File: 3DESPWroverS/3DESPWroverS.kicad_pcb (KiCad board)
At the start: 2 copper layers, 40 x 40 mm, 9 parts, among them J1 Conn_02x03_Odd_Even, J2 Conn_01x01, J3 Conn_01x01, J4 Conn_01x01, J5 Conn_01x01, J6 Conn_01x01, J7 Conn_01x01, J8 Conn_01x01, J9 Conn_01x01

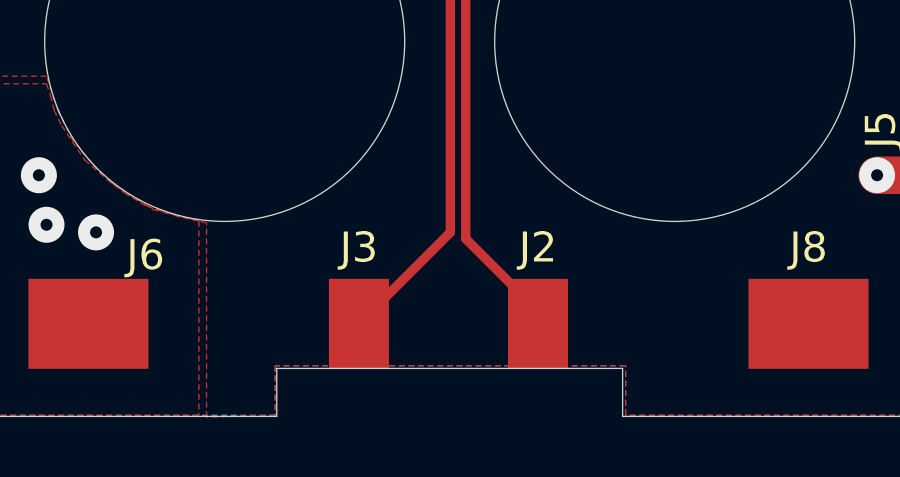
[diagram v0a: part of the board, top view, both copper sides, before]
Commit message: Correction to 3.3v regulator connection
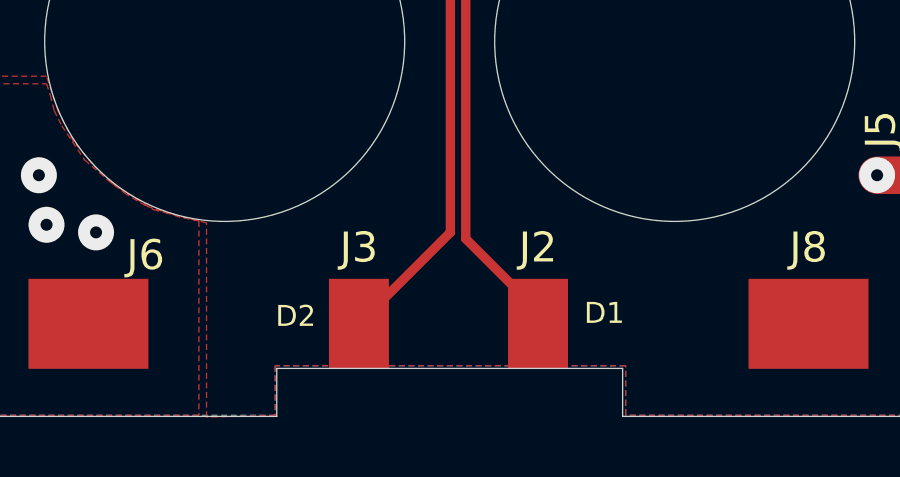
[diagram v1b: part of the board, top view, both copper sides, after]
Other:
- board text added: "D1"
- board text added: "D2"
- board text added: "GND"
- board text added: "VCC"
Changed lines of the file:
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@@
   (general
     (thickness 1.6)
-    (drawings 66)
+    (drawings 72)
     (tracks 31)
     (zones 0)
@@
       (effects (font (size 1 1) (thickness 0.15)) (justify mirror))
     )
+    (fp_line (start 4.35 1.8) (end -1.8 1.8) (layer B.CrtYd) (width 0.05))
+    (fp_line (start 4.35 -6.85) (end 4.35 1.8) (layer B.CrtYd) (width 0.05))
+    (fp_line (start -1.8 -6.85) (end 4.35 -6.85) (layer B.CrtYd) (width 0.05))
+    (fp_line (start -1.8 1.8) (end -1.8 -6.85) (layer B.CrtYd) (width 0.05))
+    (fp_line (start -1.33 1.33) (end 0 1.33) (layer B.SilkS) (width 0.12))
+    (fp_line (start -1.33 0) (end -1.33 1.33) (layer B.SilkS) (width 0.12))
+    (fp_line (start 1.27 1.33) (end 3.87 1.33) (layer B.SilkS) (width 0.12))
+    (fp_line (start 1.27 -1.27) (end 1.27 1.33) (layer B.SilkS) (width 0.12))
+    (fp_line (start -1.33 -1.27) (end 1.27 -1.27) (layer B.SilkS) (width 0.12))
+    (fp_line (start 3.87 1.33) (end 3.87 -6.41) (layer B.SilkS) (width 0.12))
+    (fp_line (start -1.33 -1.27) (end -1.33 -6.41) (layer B.SilkS) (width 0.12))
+    (fp_line (start -1.33 -6.41) (end 3.87 -6.41) (layer B.SilkS) (width 0.12))
+    (fp_line (start -1.27 0) (end 0 1.27) (layer B.Fab) (width 0.1))
+    (fp_line (start -1.27 -6.35) (end -1.27 0) (layer B.Fab) (width 0.1))
+    (fp_line (start 3.81 -6.35) (end -1.27 -6.35) (layer B.Fab) (width 0.1))
+    (fp_line (start 3.81 1.27) (end 3.81 -6.35) (layer B.Fab) (width 0.1))
     (fp_line (start 0 1.27) (end 3.81 1.27) (layer B.Fab) (width 0.1))
-    (fp_line (start 3.81 1.27) (end 3.81 -6.35) (layer B.Fab) (width 0.1))
-    (fp_line (start 3.81 -6.35) (end -1.27 -6.35) (layer B.Fab) (width 0.1))
-    (fp_line (start -1.27 -6.35) (end -1.27 0) (layer B.Fab) (width 0.1))
-    (fp_line (start -1.27 0) (end 0 1.27) (layer B.Fab) (width 0.1))
-    (fp_line (start -1.33 -6.41) (end 3.87 -6.41) (layer B.SilkS) (width 0.12))
-    (fp_line (start -1.33 -1.27) (end -1.33 -6.41) (layer B.SilkS) (width 0.12))
-    (fp_line (start 3.87 1.33) (end 3.87 -6.41) (layer B.SilkS) (width 0.12))
-    (fp_line (start -1.33 -1.27) (end 1.27 -1.27) (layer B.SilkS) (width 0.12))
-    (fp_line (start 1.27 -1.27) (end 1.27 1.33) (layer B.SilkS) (width 0.12))
-    (fp_line (start 1.27 1.33) (end 3.87 1.33) (layer B.SilkS) (width 0.12))
-    (fp_line (start -1.33 0) (end -1.33 1.33) (layer B.SilkS) (width 0.12))
-    (fp_line (start -1.33 1.33) (end 0 1.33) (layer B.SilkS) (width 0.12))
-    (fp_line (start -1.8 1.8) (end -1.8 -6.85) (layer B.CrtYd) (width 0.05))
-    (fp_line (start -1.8 -6.85) (end 4.35 -6.85) (layer B.CrtYd) (width 0.05))
-    (fp_line (start 4.35 -6.85) (end 4.35 1.8) (layer B.CrtYd) (width 0.05))
-    (fp_line (start 4.35 1.8) (end -1.8 1.8) (layer B.CrtYd) (width 0.05))
     (fp_text user %R (at 1.27 -2.54) (layer B.Fab)
       (effects (font (size 1 1) (thickness 0.15)) (justify mirror))
@@
       (net 2 GND))
   )
+  (gr_text D2 (at 115.3668 74.549) (layer F.SilkS)
+    (effects (font (size 0.7 0.7) (thickness 0.15)))
+  )
+  (gr_text D1 (at 125.6538 74.4474) (layer F.SilkS)
+    (effects (font (size 0.7 0.7) (thickness 0.15)))
+  )
+  (gr_text GND (at 120.5992 62.7126) (layer B.SilkS)
+    (effects (font (size 0.7 0.7) (thickness 0.15)) (justify mirror))
+  )
+  (gr_text D2 (at 120.4722 61.4934) (layer B.SilkS)
+    (effects (font (size 0.7 0.7) (thickness 0.15)) (justify mirror))
+  )
+  (gr_text D1 (at 120.4976 54.0766) (layer B.SilkS)
+    (effects (font (size 0.7 0.7) (thickness 0.15)) (justify mirror))
+  )
+  (gr_text VCC (at 120.4976 52.6034) (layer B.SilkS)
+    (effects (font (size 0.7 0.7) (thickness 0.15)) (justify mirror))
+  )
   (gr_line (start 107.3 41.579) (end 107.3 43.489) (layer Edge.Cuts) (width 0.02))
   (gr_line (start 106.74 41.579) (end 106.74 43.489) (layer Dwgs.User) (width 0.02))
@@
   (gr_line (start 103.84 41.579) (end 107.3 41.579) (layer Edge.Cuts) (width 0.02))
   (gr_line (start 103.84 41.579) (end 103.84 43.489) (layer Edge.Cuts) (width 0.02))
-  (gr_text "Project Cube, v1.1\nREAL, ITU\nrodr" (at 102.616 42.291) (layer B.SilkS)
-    (effects (font (size 1 1) (thickness 0.15)) (justify right mirror))
+  (gr_text "Project Cube, v1.1\nREAL, ITU\nrodr" (at 120.5992 43.3324) (layer B.SilkS)
+    (effects (font (size 1 1) (thickness 0.15)) (justify mirror))
   )
   (gr_line (start 102.1 47.889) (end 102.1 43.889) (layer Edge.Cuts) (width 0.02))

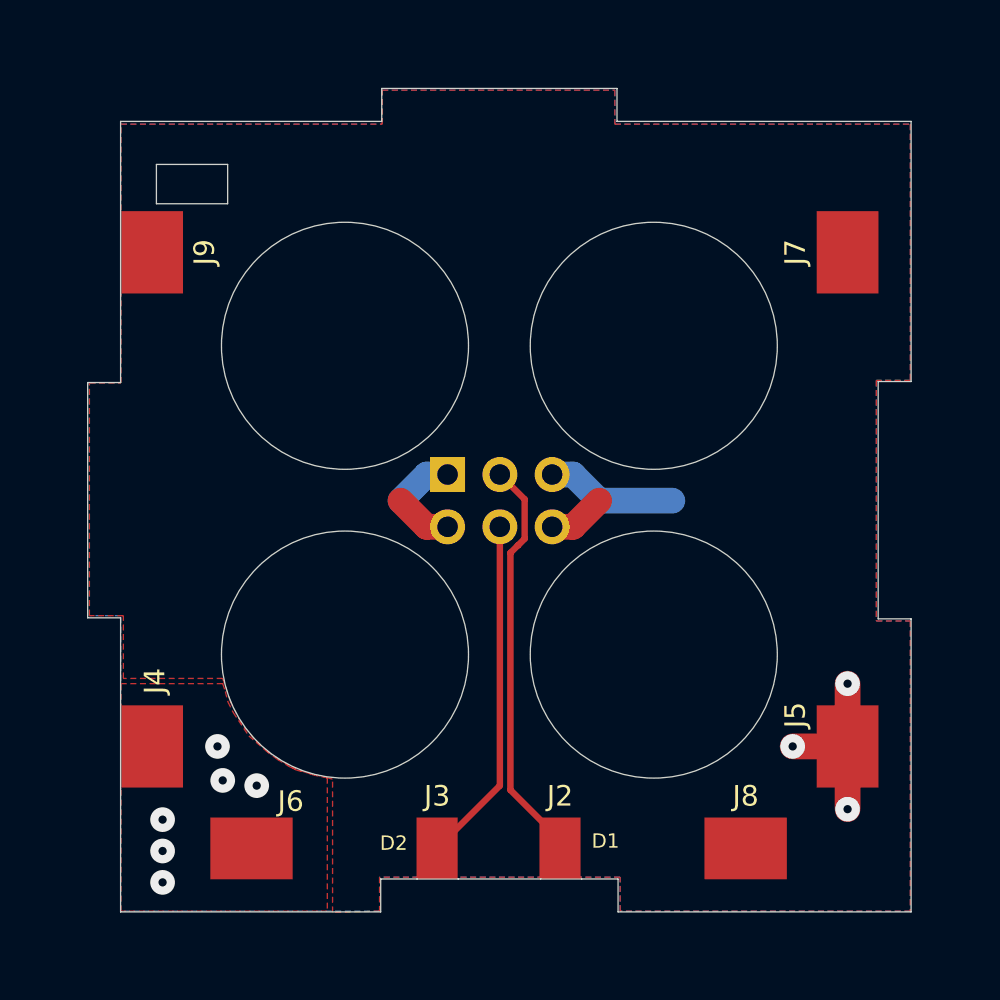
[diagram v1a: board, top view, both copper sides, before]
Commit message: Corrected switching step down power source connections and added mill corner paths
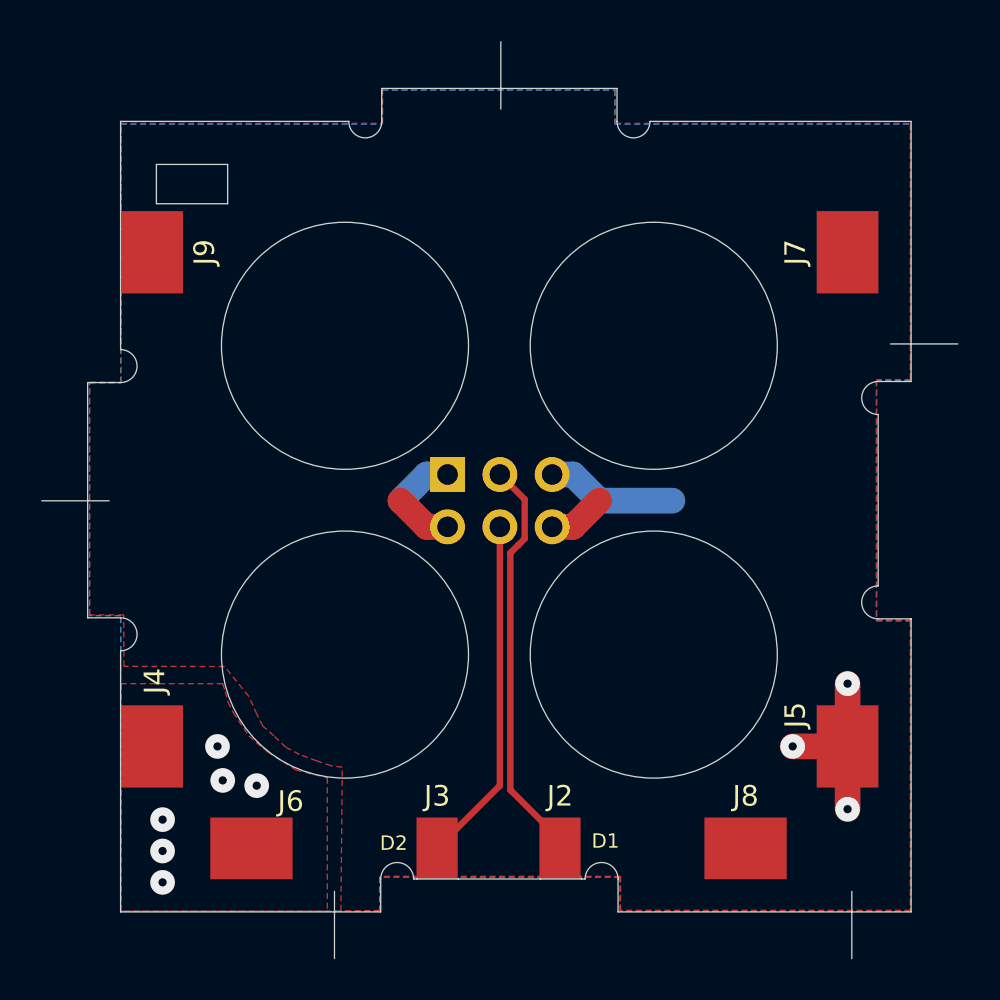
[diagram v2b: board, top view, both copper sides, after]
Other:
- board size 40 x 40 mm -> 44.5 x 44.5 mm
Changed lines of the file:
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@@
   (general
     (thickness 1.6)
-    (drawings 72)
+    (drawings 85)
     (tracks 31)
     (zones 0)
@@
       (net 2 GND))
   )
+  (gr_line (start 112.49 76.89) (end 112.49 80.16) (layer Edge.Cuts) (width 0.05588))
+  (gr_line (start 137.62 76.89) (end 137.62 80.16) (layer Edge.Cuts) (width 0.05588))
+  (gr_line (start 101.54 57.92) (end 98.27 57.92) (layer Edge.Cuts) (width 0.05588))
+  (gr_line (start 120.57 38.89) (end 120.57 35.62) (layer Edge.Cuts) (width 0.05588))
+  (gr_line (start 139.5 50.3) (end 142.77 50.3) (layer Edge.Cuts) (width 0.05588))
+  (gr_arc (start 138.9 52.924715) (end 138.9 52.124715) (angle -180) (layer Edge.Cuts) (width 0.02))
+  (gr_arc (start 125.464285 76.289) (end 126.264285 76.289) (angle -180) (layer Edge.Cuts) (width 0.02))
+  (gr_arc (start 138.9 62.853285) (end 138.9 62.053285) (angle -180) (layer Edge.Cuts) (width 0.02))
+  (gr_arc (start 115.535715 76.288999) (end 116.335715 76.288999) (angle -180) (layer Edge.Cuts) (width 0.02))
+  (gr_arc (start 113.985715 39.489) (end 113.185715 39.489) (angle -180) (layer Edge.Cuts) (width 0.02))
+  (gr_arc (start 102.1 64.403285) (end 102.1 65.203285) (angle -180) (layer Edge.Cuts) (width 0.02))
+  (gr_arc (start 102.1 51.374715) (end 102.1 52.174715) (angle -180) (layer Edge.Cuts) (width 0.02))
+  (gr_arc (start 127.014285 39.489) (end 126.214285 39.489) (angle -180) (layer Edge.Cuts) (width 0.02))
   (gr_text D2 (at 115.3668 74.549) (layer F.SilkS)
     (effects (font (size 0.7 0.7) (thickness 0.15)))
@@
   (gr_circle (center 127.999999 50.389001) (end 121.999999 50.389001) (layer Edge.Cuts) (width 0.02))
   (gr_circle (center 127.999999 65.389) (end 121.999999 65.389) (layer Edge.Cuts) (width 0.02))
-  (gr_line (start 126.264285 76.289) (end 124.5 76.288999) (layer Edge.Cuts) (width 0.02))
+  (gr_line (start 124.664285 76.289) (end 124.5 76.288999) (layer Edge.Cuts) (width 0.02))
   (gr_line (start 126.264285 77.889) (end 126.264285 76.289) (layer Edge.Cuts) (width 0.02))
   (gr_line (start 140.5 77.889) (end 126.264285 77.889) (layer Edge.Cuts) (width 0.02))
   (gr_line (start 140.5 63.653285) (end 140.5 77.889) (layer Edge.Cuts) (width 0.02))
   (gr_line (start 138.9 63.653285) (end 140.5 63.653285) (layer Edge.Cuts) (width 0.02))
-  (gr_line (start 138.9 52.124715) (end 138.9 63.653285) (layer Edge.Cuts) (width 0.02))
+  (gr_line (start 138.9 53.724715) (end 138.9 62.053285) (layer Edge.Cuts) (width 0.02))
   (gr_line (start 140.5 52.124715) (end 138.9 52.124715) (layer Edge.Cuts) (width 0.02))
   (gr_line (start 140.5 39.489001) (end 140.5 52.124715) (layer Edge.Cuts) (width 0.02))
-  (gr_line (start 126.214285 39.489) (end 140.5 39.489001) (layer Edge.Cuts) (width 0.02))
+  (gr_line (start 127.814285 39.489) (end 140.5 39.489) (layer Edge.Cuts) (width 0.02))
   (gr_line (start 126.214285 37.889) (end 126.214285 39.489) (layer Edge.Cuts) (width 0.02))
   (gr_line (start 114.785715 37.889) (end 126.214285 37.889) (layer Edge.Cuts) (width 0.02))
   (gr_line (start 114.785715 39.489) (end 114.785715 37.889) (layer Edge.Cuts) (width 0.02))
-  (gr_line (start 102.1 39.489) (end 114.785715 39.489) (layer Edge.Cuts) (width 0.02))
+  (gr_line (start 102.1 39.489) (end 113.185715 39.489) (layer Edge.Cuts) (width 0.02))
   (gr_line (start 102.1 43.889) (end 102.1 39.489) (layer Edge.Cuts) (width 0.02))
   (gr_line (start 105.1 43.889) (end 102.1 43.889) (layer Dwgs.User) (width 0.2))
   (gr_line (start 105.1 47.889) (end 105.1 43.889) (layer Dwgs.User) (width 0.2))
   (gr_line (start 102.1 47.889) (end 105.1 47.889) (layer Dwgs.User) (width 0.2))
-  (gr_line (start 102.1 52.174715) (end 102.1 47.889) (layer Edge.Cuts) (width 0.02))
+  (gr_line (start 102.1 50.574715) (end 102.1 47.889) (layer Edge.Cuts) (width 0.02))
   (gr_line (start 100.5 52.174715) (end 102.1 52.174715) (layer Edge.Cuts) (width 0.02))
   (gr_line (start 100.5 63.603285) (end 100.5 52.174715) (layer Edge.Cuts) (width 0.02))
   (gr_line (start 102.1 63.603285) (end 100.5 63.603285) (layer Edge.Cuts) (width 0.02))
-  (gr_line (start 102.1 67.889) (end 102.1 63.603285) (layer Edge.Cuts) (width 0.02))
+  (gr_line (start 102.1 67.889) (end 102.1 65.203285) (layer Edge.Cuts) (width 0.02))
   (gr_line (start 105.100001 67.889) (end 102.1 67.889) (layer Dwgs.User) (width 0.2))
   (gr_line (start 105.100001 71.889) (end 105.100001 67.889) (layer Dwgs.User) (width 0.2))
@@
   (gr_line (start 114.735715 77.889) (end 102.1 77.889) (layer Edge.Cuts) (width 0.02))
   (gr_line (start 114.735715 76.288999) (end 114.735715 77.889) (layer Edge.Cuts) (width 0.02))
-  (gr_line (start 116.5 76.288999) (end 114.735715 76.288999) (layer Edge.Cuts) (width 0.02))
+  (gr_line (start 116.5 76.288999) (end 116.335715 76.288999) (layer Edge.Cuts) (width 0.02))
   (gr_line (start 116.5 73.288999) (end 116.5 76.288999) (layer Dwgs.User) (width 0.2))
   (gr_line (start 118.5 73.288999) (end 116.5 73.288999) (layer Dwgs.User) (width 0.2))
@@
     (polygon
       (pts
-        (xy 126.365 76.2) (xy 114.681 76.2) (xy 114.681 77.851) (xy 112.395 77.9145) (xy 112.395 71.4375)
-        (xy 112.141 71.374) (xy 111.506 71.247) (xy 110.363 70.866) (xy 109.728 70.485) (xy 109.22 70.104)
-        (xy 108.585 69.469) (xy 107.95 68.707) (xy 107.442 67.691) (xy 107.061 66.548) (xy 102.235 66.548)
-        (xy 102.235 63.5) (xy 100.584 63.5) (xy 100.584 52.197) (xy 102.108 52.197) (xy 102.108 39.624)
-        (xy 114.808 39.624) (xy 114.808 37.973) (xy 126.111 37.973) (xy 126.111 39.624) (xy 140.462 39.624)
-        (xy 140.462 52.07) (xy 138.811 52.07) (xy 138.811 63.754) (xy 140.462 63.754) (xy 140.462 77.851)
-        (xy 126.365 77.851)
+        (xy 126.385 76.16) (xy 114.701 76.16) (xy 114.701 77.811) (xy 112.8 77.84) (xy 112.87 70.86)
+        (xy 112.33 70.79) (xy 111.62 70.55) (xy 110.79 70.24) (xy 110.13 69.89) (xy 109.55 69.34)
+        (xy 109.01 68.86) (xy 108.72 68.29) (xy 108.325 67.415) (xy 107.15 65.97) (xy 102.26 65.96)
+        (xy 102.255 63.46) (xy 100.604 63.46) (xy 100.604 52.157) (xy 102.128 52.157) (xy 102.128 39.584)
+        (xy 114.828 39.584) (xy 114.828 37.933) (xy 126.131 37.933) (xy 126.131 39.584) (xy 140.482 39.584)
+        (xy 140.482 52.03) (xy 138.831 52.03) (xy 138.831 63.714) (xy 140.482 63.714) (xy 140.482 77.811)
+        (xy 126.385 77.811)
       )
     )

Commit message: Ordered
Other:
- board text added: "Project Cube, v1.2 REAL, ITU"
- board text removed: "Project Cube, v1.1 REAL, ITU rodr"
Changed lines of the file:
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@@
       (effects (font (size 1 1) (thickness 0.15)) (justify mirror))
     )
+    (fp_line (start 0 1.27) (end 3.81 1.27) (layer B.Fab) (width 0.1))
+    (fp_line (start 3.81 1.27) (end 3.81 -6.35) (layer B.Fab) (width 0.1))
+    (fp_line (start 3.81 -6.35) (end -1.27 -6.35) (layer B.Fab) (width 0.1))
+    (fp_line (start -1.27 -6.35) (end -1.27 0) (layer B.Fab) (width 0.1))
+    (fp_line (start -1.27 0) (end 0 1.27) (layer B.Fab) (width 0.1))
+    (fp_line (start -1.33 -6.41) (end 3.87 -6.41) (layer B.SilkS) (width 0.12))
+    (fp_line (start -1.33 -1.27) (end -1.33 -6.41) (layer B.SilkS) (width 0.12))
+    (fp_line (start 3.87 1.33) (end 3.87 -6.41) (layer B.SilkS) (width 0.12))
+    (fp_line (start -1.33 -1.27) (end 1.27 -1.27) (layer B.SilkS) (width 0.12))
+    (fp_line (start 1.27 -1.27) (end 1.27 1.33) (layer B.SilkS) (width 0.12))
+    (fp_line (start 1.27 1.33) (end 3.87 1.33) (layer B.SilkS) (width 0.12))
+    (fp_line (start -1.33 0) (end -1.33 1.33) (layer B.SilkS) (width 0.12))
+    (fp_line (start -1.33 1.33) (end 0 1.33) (layer B.SilkS) (width 0.12))
+    (fp_line (start -1.8 1.8) (end -1.8 -6.85) (layer B.CrtYd) (width 0.05))
+    (fp_line (start -1.8 -6.85) (end 4.35 -6.85) (layer B.CrtYd) (width 0.05))
+    (fp_line (start 4.35 -6.85) (end 4.35 1.8) (layer B.CrtYd) (width 0.05))
     (fp_line (start 4.35 1.8) (end -1.8 1.8) (layer B.CrtYd) (width 0.05))
-    (fp_line (start 4.35 -6.85) (end 4.35 1.8) (layer B.CrtYd) (width 0.05))
-    (fp_line (start -1.8 -6.85) (end 4.35 -6.85) (layer B.CrtYd) (width 0.05))
-    (fp_line (start -1.8 1.8) (end -1.8 -6.85) (layer B.CrtYd) (width 0.05))
-    (fp_line (start -1.33 1.33) (end 0 1.33) (layer B.SilkS) (width 0.12))
-    (fp_line (start -1.33 0) (end -1.33 1.33) (layer B.SilkS) (width 0.12))
-    (fp_line (start 1.27 1.33) (end 3.87 1.33) (layer B.SilkS) (width 0.12))
-    (fp_line (start 1.27 -1.27) (end 1.27 1.33) (layer B.SilkS) (width 0.12))
-    (fp_line (start -1.33 -1.27) (end 1.27 -1.27) (layer B.SilkS) (width 0.12))
-    (fp_line (start 3.87 1.33) (end 3.87 -6.41) (layer B.SilkS) (width 0.12))
-    (fp_line (start -1.33 -1.27) (end -1.33 -6.41) (layer B.SilkS) (width 0.12))
-    (fp_line (start -1.33 -6.41) (end 3.87 -6.41) (layer B.SilkS) (width 0.12))
-    (fp_line (start -1.27 0) (end 0 1.27) (layer B.Fab) (width 0.1))
-    (fp_line (start -1.27 -6.35) (end -1.27 0) (layer B.Fab) (width 0.1))
-    (fp_line (start 3.81 -6.35) (end -1.27 -6.35) (layer B.Fab) (width 0.1))
-    (fp_line (start 3.81 1.27) (end 3.81 -6.35) (layer B.Fab) (width 0.1))
-    (fp_line (start 0 1.27) (end 3.81 1.27) (layer B.Fab) (width 0.1))
     (fp_text user %R (at 1.27 -2.54) (layer B.Fab)
       (effects (font (size 1 1) (thickness 0.15)) (justify mirror))
@@
   (gr_line (start 103.84 41.579) (end 107.3 41.579) (layer Edge.Cuts) (width 0.02))
   (gr_line (start 103.84 41.579) (end 103.84 43.489) (layer Edge.Cuts) (width 0.02))
-  (gr_text "Project Cube, v1.1\nREAL, ITU\nrodr" (at 120.5992 43.3324) (layer B.SilkS)
+  (gr_text "Project Cube, v1.2\nREAL, ITU" (at 120.5992 43.3324) (layer B.SilkS)
     (effects (font (size 1 1) (thickness 0.15)) (justify mirror))
   )
